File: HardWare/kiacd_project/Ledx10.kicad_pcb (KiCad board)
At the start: 2 copper layers, 160 x 160 mm, 60 parts, among them J1 POWER_IN, U1 TPS923651

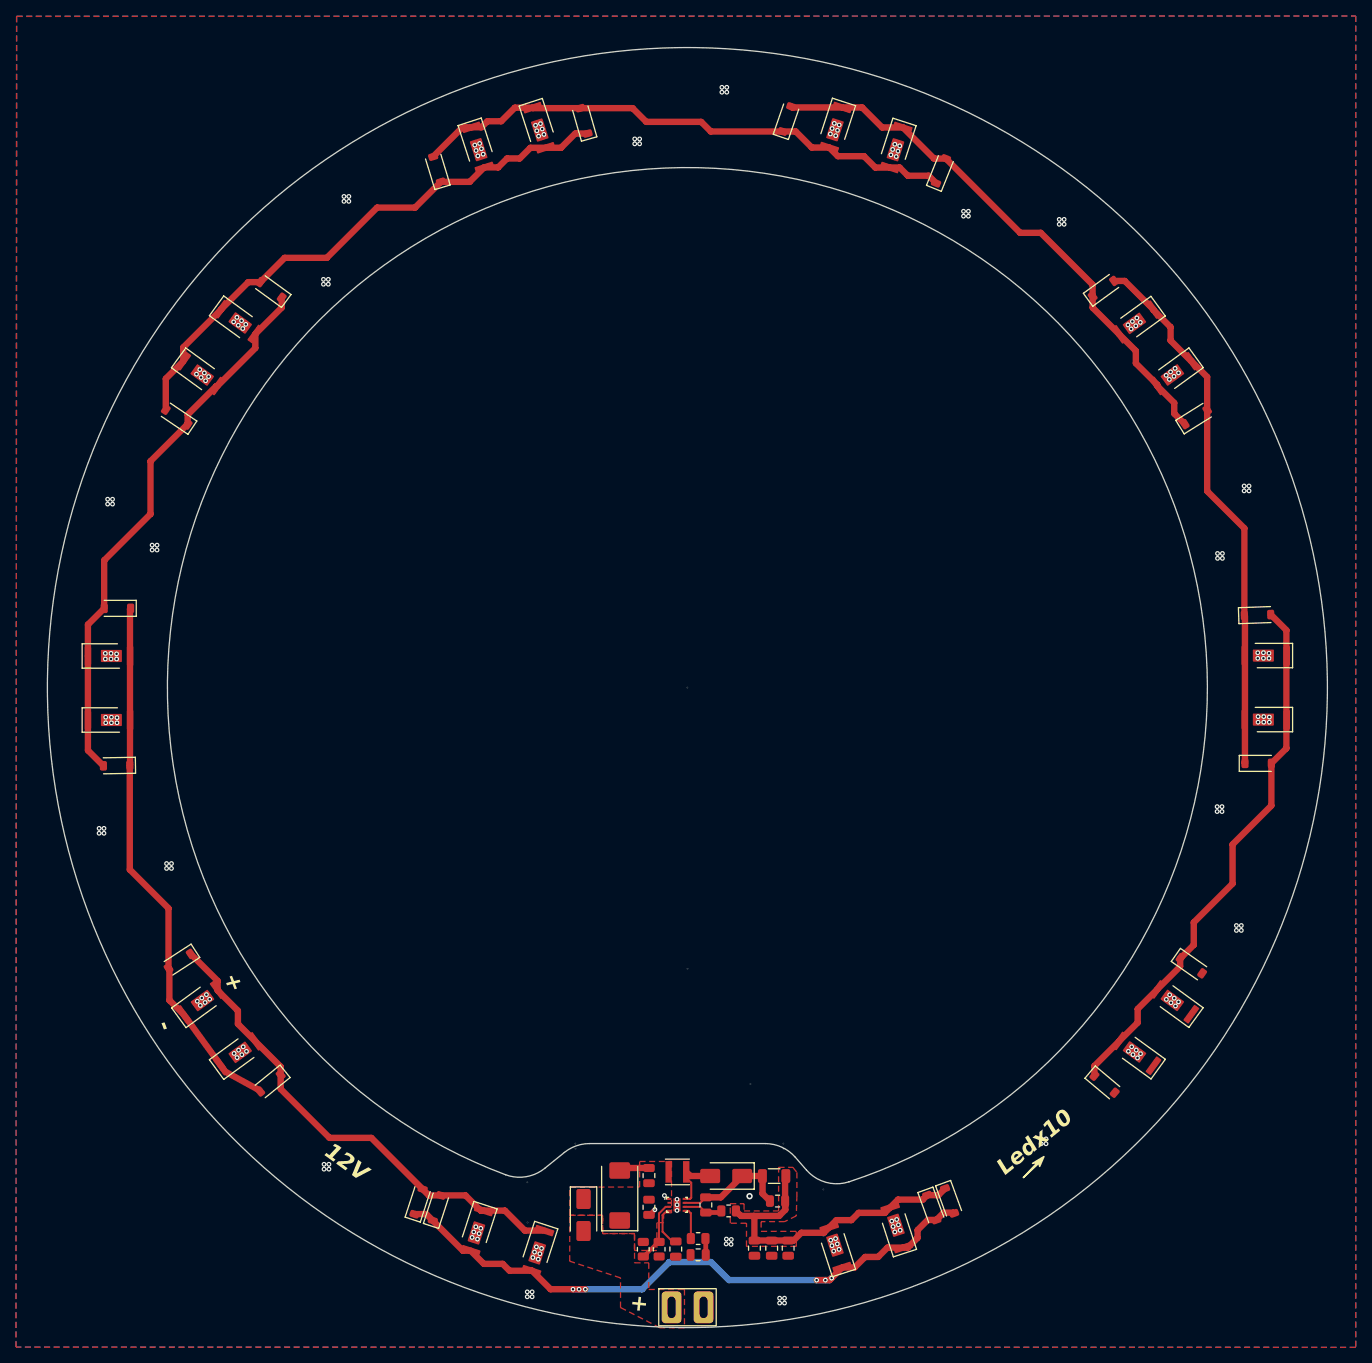
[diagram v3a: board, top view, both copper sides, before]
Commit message: 更新LED5730封装错误，手册没有说明散热焊盘与阳极相连
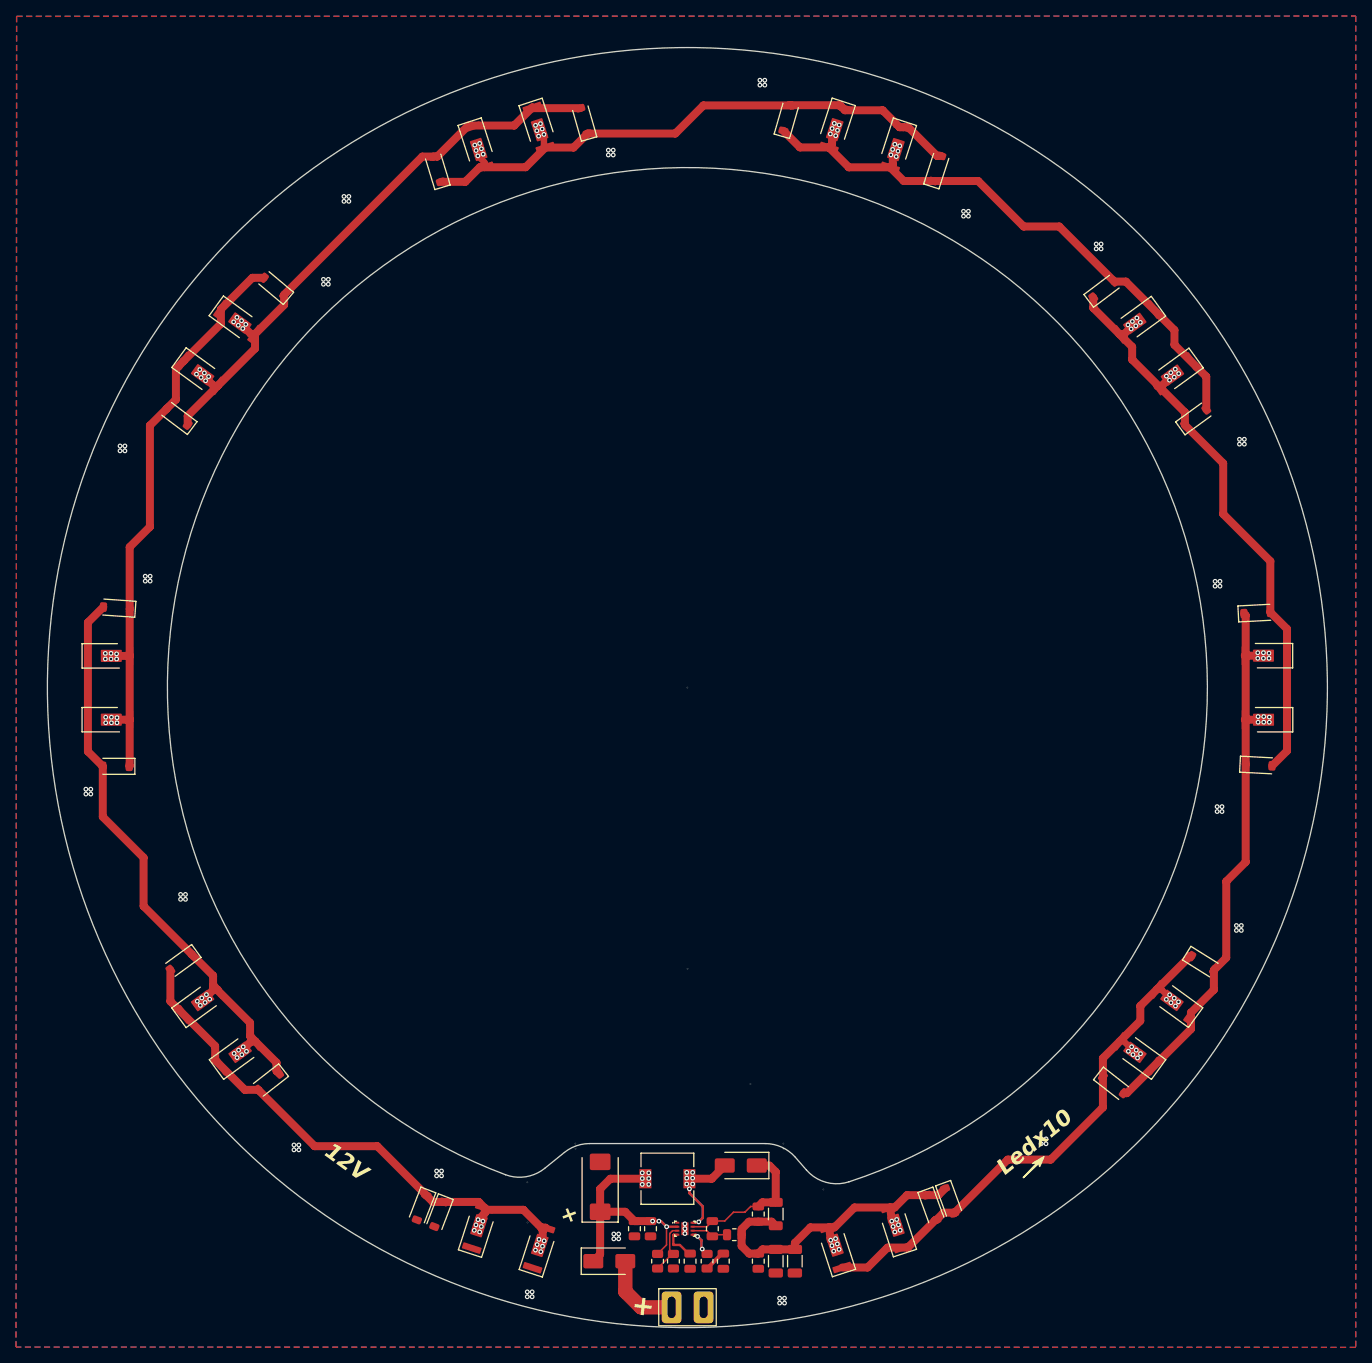
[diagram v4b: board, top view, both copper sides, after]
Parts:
- C10, C9: footprint Capacitor_SMD:C_0805_2012Metric -> Capacitor_SMD:C_1206_3216Metric
- L1: value SCL3216T330KSP,33uH -> SMMS0650-680M,68uH; footprint Inductor_SMD:L_Taiyo-Yuden_MD-3030 -> Inductor_SMD:L_6.3x6.3_H3
- moved D23 137.2 mm to (25.8, 93.4), turned to 0 degrees
- moved D39 137.2 mm to (153.7, 51.9), turned to -144 degrees
- moved D7 137.2 mm to (169.8, 101.4), turned to 180 degrees
- moved D10 137.2 mm to (158.4, 58.3), turned to -144 degrees
- moved D34 137.2 mm to (41.9, 143.0), turned to 36 degrees
- moved D40 137.2 mm to (169.8, 93.4), turned to 180 degrees
- moved D26 137.2 mm to (37.2, 136.5), turned to 36 degrees
- moved D35 137.2 mm to (25.8, 101.4), turned to 0 degrees
- moved D9 137.1 mm to (169.3, 107.1), turned to -3 degrees
- moved D25 137.1 mm to (26.4, 107.2), turned to 180 degrees
- moved D24 137.0 mm to (26.5, 87.4), turned to 176 degrees
- moved D12 137.0 mm to (149.9, 47.6), turned to 37 degrees
- moved D27 136.9 mm to (34.5, 131.7), turned to -144 degrees
- moved D11 136.9 mm to (161.3, 63.6), turned to 36 degrees
- moved D28 136.7 mm to (45.5, 146.7), turned to -142 degrees
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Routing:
- net VCC: track 0.00 -> 31.9 mm, vias 0 -> 9
- net Net-(D10-A): track 53.6 -> 74.3 mm, vias 0 -> 12
- net Net-(D1-K): track 81.3 -> 69.0 mm, vias 6 -> 12
- net Net-(D32-A): track 0.00 -> 10.4 mm
- net Net-(D19-A): track 7.58 -> 17.3 mm, vias 0 -> 8
- net Net-(D4-K): track 61.9 -> 71.2 mm, vias 0 -> 12
- net Net-(D10-K): track 69.5 -> 75.8 mm, vias 0 -> 12
- net Net-(D23-K): track 68.0 -> 73.9 mm, vias 0 -> 12
- net GND: track 5.59 -> 0.33 mm, vias 202 -> 83
- net Net-(D20-K): track 69.1 -> 73.6 mm, vias 0 -> 12
- net Net-(D16-K): track 69.3 -> 72.9 mm, vias 0 -> 12
- net Net-(D19-K): track 14.6 -> 18.2 mm
- net Net-(D13-K): track 70.3 -> 72.7 mm, vias 0 -> 12
- net Net-(U1-DIM): track 8.30 -> 6.57 mm
- net Net-(U1-COMP): track 4.07 -> 5.21 mm, vias 0 -> 2
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- removed copper zone on F.Cu, net /LED+
- removed copper zone on F.Cu, net Net-(D32-A)
- removed copper zone on F.Cu, net VCC
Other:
- outline, holes or cut-outs redrawn
- board text added: "TPS9235x Led Driver"
- board text removed: "-"
- board text removed: "TPS92x Led Driver"
